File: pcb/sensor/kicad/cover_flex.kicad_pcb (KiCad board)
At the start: 2 copper layers, 31.1 x 29.1 mm, 7 parts, among them J1 +5V pin pad, J2 GND pin pad, J3 S7081-42R VBAT, J4 S7081-42R GND, U1 TLV75533PDBVR

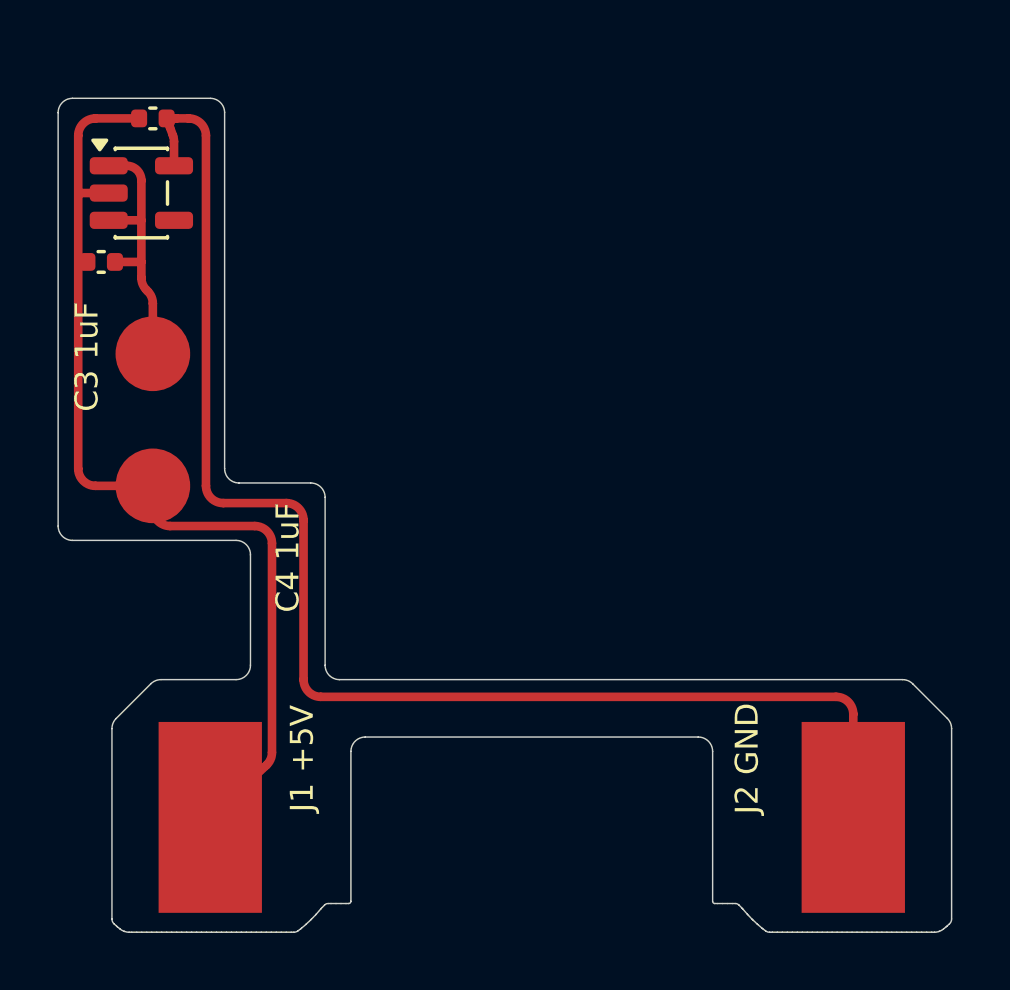
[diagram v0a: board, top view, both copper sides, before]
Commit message: Flex review fixes, back cover clip, README, Sladdseg, order lists (D-116..D-119)
- D-116: cover flex: 0603 X5R input/output caps, ESD diode TPD1E10B06DYAR,
  0.6 mm bend radius with relief slits, stiffener notch and outlines,
  coverlay expansion, mask-defined pin pads, teardrops, fab notes; the
  cover's snap hooks allow for stiffener adhesive and tolerance
- D-117, D-118: bottom clip catch 3.22 above the floor, tip as far proud of
  the shell as the top clip's
- Battery polarity confirmed on a unit
- README rewritten: three editions, assembly renders, safety and polarity
  warnings, cost for 1 to 10,000 plates, printed parts; detail and board
  renders moved to their docs; the product is named Sladdseg
- EU boards: the ant logo on the other face
- D-119: order lists: one NA plate, one EU plate, a devkit of 5 + 5
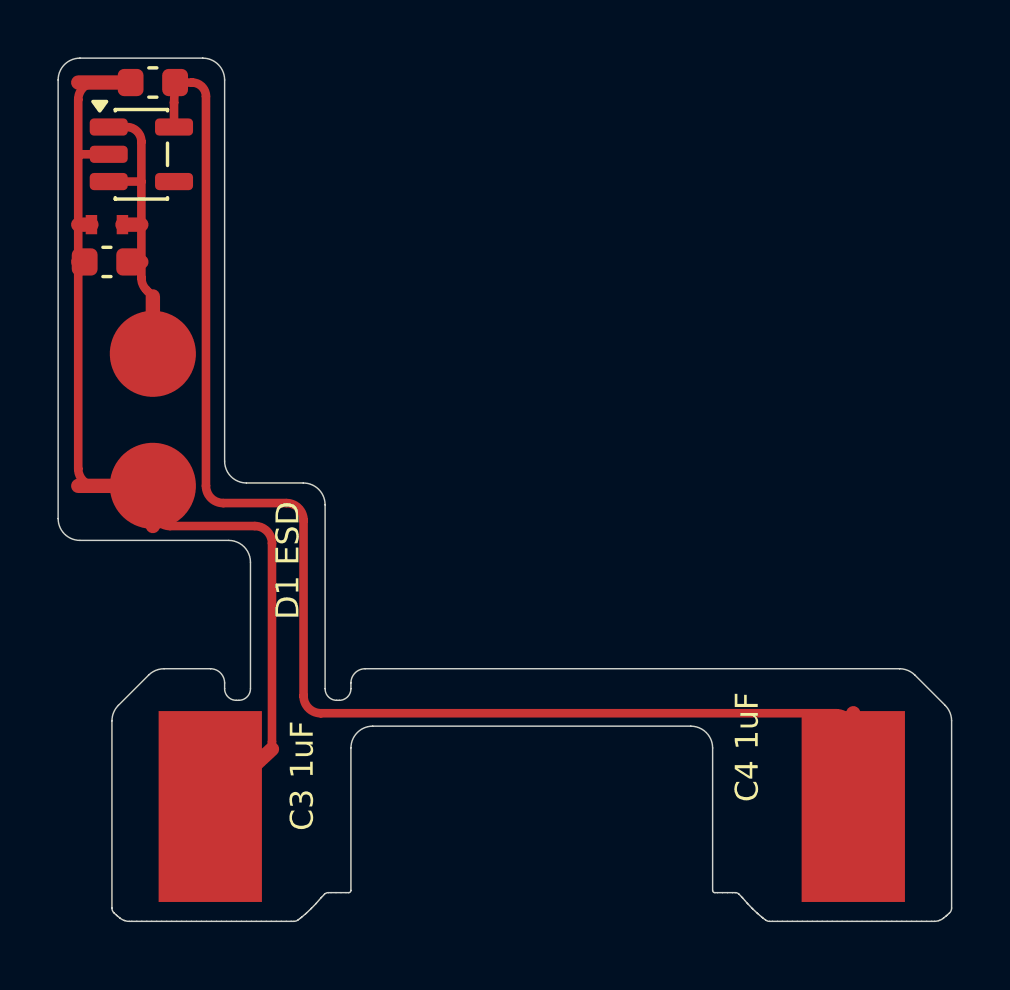
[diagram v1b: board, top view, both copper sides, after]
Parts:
- added D1: TPD1E10B06DYAR, sensor:D_SOD-523_TI_DYA0002A, F.Cu at (85.2, 104.4)
- C3, C4: value 1uF -> 1uF 16V X5R 0603; footprint sensor:C_0402_1005Metric -> sensor:C_0603_1608Metric
- moved U1 1.35 mm to (86.4, 102.0)
- moved C4 1.25 mm to (86.8, 99.5)
- moved J3 0.38 mm to (111.2, 124.7)
- moved J4 0.38 mm to (88.8, 124.7)
- moved C3 0.20 mm to (85.2, 105.7)
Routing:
- net GND: track 34.4 -> 44.8 mm
- net +5V: track 9.61 -> 14.2 mm
- net +3V3: track 48.3 -> 52.2 mm
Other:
- board size 31.1 x 29.1 mm -> 31.1 x 30.1 mm
- rule pad_to_mask_clearance: 0 -> 0.1
- board text added: "1 copper layer flex: polyimide, 0.10 mm without stiffeners, 1/2 oz Cu, yellow coverlay, ENIG"
- board text added: "BEND ZONE 90 deg, inside r 0.6 mm, copper outside"
- board text added: "BOTTOM STIFFENER FR4 0.4 mm"
- board text added: "BOTTOM STIFFENER FR4 0.8 mm"
- board text added: "Coverlay openings 0.1 mm beyond the pads; no holes"
- board text added: "D1 ESD"
- board text added: "FIT-TEST PROTOTYPE: positions REF / MEASURE"
- board text added: "FR4 stiffeners on the bottom (non-copper) side: 0.8 mm and 0.4 mm, outlines on User_1"
- board text added: "One 90 deg bend in the run, inside r 0.6 mm, copper outside, installed once"
- board text removed: "BEND 90 deg, copper outside"
- board text removed: "POSITIONS REF / MEASURE - DO NOT FABRICATE"
- board text removed: "STIFFENER FR4 0.4 mm, back side (cut to the outline)"
- board text removed: "STIFFENER FR4 0.8 mm, back side, flush with the long edges (snap hooks)"
